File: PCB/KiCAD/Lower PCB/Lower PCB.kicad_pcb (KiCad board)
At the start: 2 copper layers, 188.6 x 165.4 mm, 114 parts, among them IC1 ADG608BRZ, IC2 ADG608BRZ, IC3 ADG608BRZ, Q1 SFH320, Q10 SFH320, Q11 SFH320, Q12 SFH320, Q13 SFH320, Q14 SFH320, Q15 SFH320, Q16 SFH320, Q17 SFH320, Q18 SFH320, Q19 SFH320, Q2 SFH320, Q20 SFH320, Q21 SFH320, Q22 SFH320, Q23 SFH320, Q24 SFH320, Q3 SFH320, Q4 SFH320, Q5 SFH320, Q6 SFH320, Q7 SFH320, Q8 SFH320, Q9 SFH320

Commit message: Work on the lower PCB
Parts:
- added J1: Conn_01x04_MountingPin, Connector_JST:JST_PH_B4B-PH-SM4-TB_1x04-1MP_P2.00mm_Vertical, F.Cu at (-23.8, 40.2)
- added J2: Conn_01x04_MountingPin, Connector_JST:JST_PH_B4B-PH-SM4-TB_1x04-1MP_P2.00mm_Vertical, F.Cu at (-54.6, -19.5)
- added J3: Conn_01x04_MountingPin, Connector_JST:JST_PH_B4B-PH-SM4-TB_1x04-1MP_P2.00mm_Vertical, F.Cu at (62.1, -1.75)
- added J4: Conn_01x02_MountingPin, Connector_JST:JST_PH_B2B-PH-SM4-TB_1x02-1MP_P2.00mm_Vertical, F.Cu at (-35.9, 40.0)
- moved D21 12.8 mm to (-107.0, -89.8)
- moved D22 12.8 mm to (-107.0, -85.2)
- moved D23 12.8 mm to (-107.0, -80.7)
- moved D24 12.8 mm to (-107.0, -76.1)
- moved D25 12.8 mm to (-107.0, -71.5)
- moved D26 12.8 mm to (-107.0, -67.0)
- moved D27 12.8 mm to (-113.1, -89.8)
- moved D28 12.8 mm to (-113.1, -85.2)
- moved D29 12.8 mm to (-113.1, -80.7)
- moved D30 12.8 mm to (-113.1, -76.1)
- moved IC3 9.94 mm to (-73.5, -58.7)
- moved Q17 6.00 mm to (-94.2, -71.5)
- moved Q18 6.00 mm to (-94.2, -67.0)
- moved C3 4.37 mm to (-73.5, -65.5)

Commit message: Started aranging the LDRs and LEDs
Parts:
- moved IC3 129.7 mm to (49.5, -17.4)
- moved D5 74.8 mm to (-59.8, 56.5)
- moved R5 63.3 mm to (-59.8, 51.8)
- moved D10 60.9 mm to (-125.1, 13.8), turned to 0 degrees
- moved D6 57.4 mm to (-125.0, -26.3), turned to 0 degrees
- moved Q5 54.6 mm to (-125.1, 8.85), turned to 0 degrees
- moved Q8 51.4 mm to (-125.0, -21.2), turned to 0 degrees
- moved D9 49.3 mm to (-125.0, 3.75), turned to 0 degrees
- moved D7 47.0 mm to (-125.0, -16.2), turned to 0 degrees
- moved R24 46.9 mm to (-52.5, 51.8)
- moved Q6 45.7 mm to (-125.0, -1.25), turned to 0 degrees
- moved Q7 44.4 mm to (-125.0, -11.2), turned to 0 degrees
- moved D8 43.9 mm to (-125.0, -6.25)
- moved D11 41.8 mm to (-20.0, -107.0), turned to -90 degrees
- moved D15 41.7 mm to (20.0, -107.0), turned to -90 degrees
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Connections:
- IC1 pad 1: unconnected-(IC1-A0-Pad1) -> LED_1_A0
- IC1 pad 15: unconnected-(IC1-A2-Pad15) -> LED_1_A2
- IC1 pad 16: unconnected-(IC1-A1-Pad16) -> LED_1_A1
- IC1 pad 8: unconnected-(IC1-D-Pad8) -> LED_1_OUT
- IC2 pad 1: unconnected-(IC2-A0-Pad1) -> LED_2_A0
- IC2 pad 15: unconnected-(IC2-A2-Pad15) -> LED_2_A2
- IC2 pad 16: unconnected-(IC2-A1-Pad16) -> LED_2_A1
- IC2 pad 8: unconnected-(IC2-D-Pad8) -> LED_2_OUT
- IC3 pad 1: unconnected-(IC3-A0-Pad1) -> LED_3_A0
- IC3 pad 15: unconnected-(IC3-A2-Pad15) -> LED_3_A2
- IC3 pad 16: unconnected-(IC3-A1-Pad16) -> LED_3_A1
- IC3 pad 8: unconnected-(IC3-D-Pad8) -> LED_3_OUT

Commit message: More chnages to LED positions and annotations
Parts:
- moved D20 249.7 mm to (-106.8, -112.0), turned to 0 degrees
- moved D19 239.8 mm to (-106.8, -102.0), turned to 0 degrees
- moved R20 234.1 mm to (-100.8, -112.0), turned to 0 degrees
- moved D18 231.3 mm to (-106.8, -92.0), turned to 0 degrees
- moved Q16 231.1 mm to (-106.8, -77.0), turned to 0 degrees
- moved R19 226.6 mm to (-100.8, -102.0), turned to 0 degrees
- moved Q15 224.1 mm to (-106.8, -67.0), turned to 0 degrees
- moved D17 224.0 mm to (-106.8, -82.0), turned to 0 degrees
- moved R18 219.9 mm to (-100.8, -92.0), turned to 0 degrees
- moved Q14 218.5 mm to (-106.8, -57.0), turned to 0 degrees
- moved D16 218.4 mm to (-106.8, -72.0), turned to 0 degrees
- moved Q13 214.6 mm to (-106.8, -47.0), turned to 0 degrees
- moved R17 214.1 mm to (-100.8, -82.0), turned to 0 degrees
- moved R43 210.6 mm to (-82.5, -114.2)
- moved R44 210.6 mm to (-82.5, -109.2)
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- renumbered J4 to J1, J1 to J2, J2 to J3, J3 to J4, R29 to R21, R30 to R22, R31 to R23, R32 to R24, R33 to R25, R34 to R26, R35 to R27, R36 to R28, R37 to R29, R38 to R30, R21 to R31, R22 to R32, R23 to R33, R24 to R34, R25 to R35, R26 to R36, R27 to R37, R28 to R38

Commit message: Positioned LDRs and LEDs
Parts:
- removed D25, D26, D27, D28, D29, D30: LED, LED_SMD:LED_PLCC-2_3.4x3.0mm_KA
- removed R25, R26, R27, R28, R29, R30: 330, Resistor_SMD:R_0805_2012Metric_Pad1.20x1.40mm_HandSolder
- J3, J4: footprint Connector_JST:JST_PH_B4B-PH-SM4-TB_1x04-1MP_P2.00mm_Vertical -> Connector_JST:JST_PH_S4B-PH-SM4-TB_1x04-1MP_P2.00mm_Horizontal
- moved D21 256.9 mm to (62.8, 42.0), turned to -135 degrees
- moved D22 249.9 mm to (48.8, 55.5), turned to -135 degrees
- moved Q21 233.8 mm to (55.8, 49.0), turned to -135 degrees
- moved Q20 233.0 mm to (70.2, 34.5), turned to -132.33 degrees
- moved D23 232.6 mm to (28.8, 58.2)
- moved R51 232.1 mm to (75.5, 27.5)
- moved D20 229.4 mm to (76.5, 26.0), turned to -120.56 degrees
- moved Q19 224.5 mm to (81.0, 16.0), turned to -103.56 degrees
- moved R50 223.7 mm to (75.5, 17.5)
- moved Q22 222.8 mm to (39.0, 58.2)
- moved R49 221.0 mm to (75.5, 7.50)
- moved R48 218.4 mm to (75.5, -2.50)
- moved D19 218.3 mm to (83.2, 5.50), turned to -96.06 degrees
- moved D24 216.1 mm to (11.5, 58.2)
- moved R47 216.1 mm to (75.5, -12.5)
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
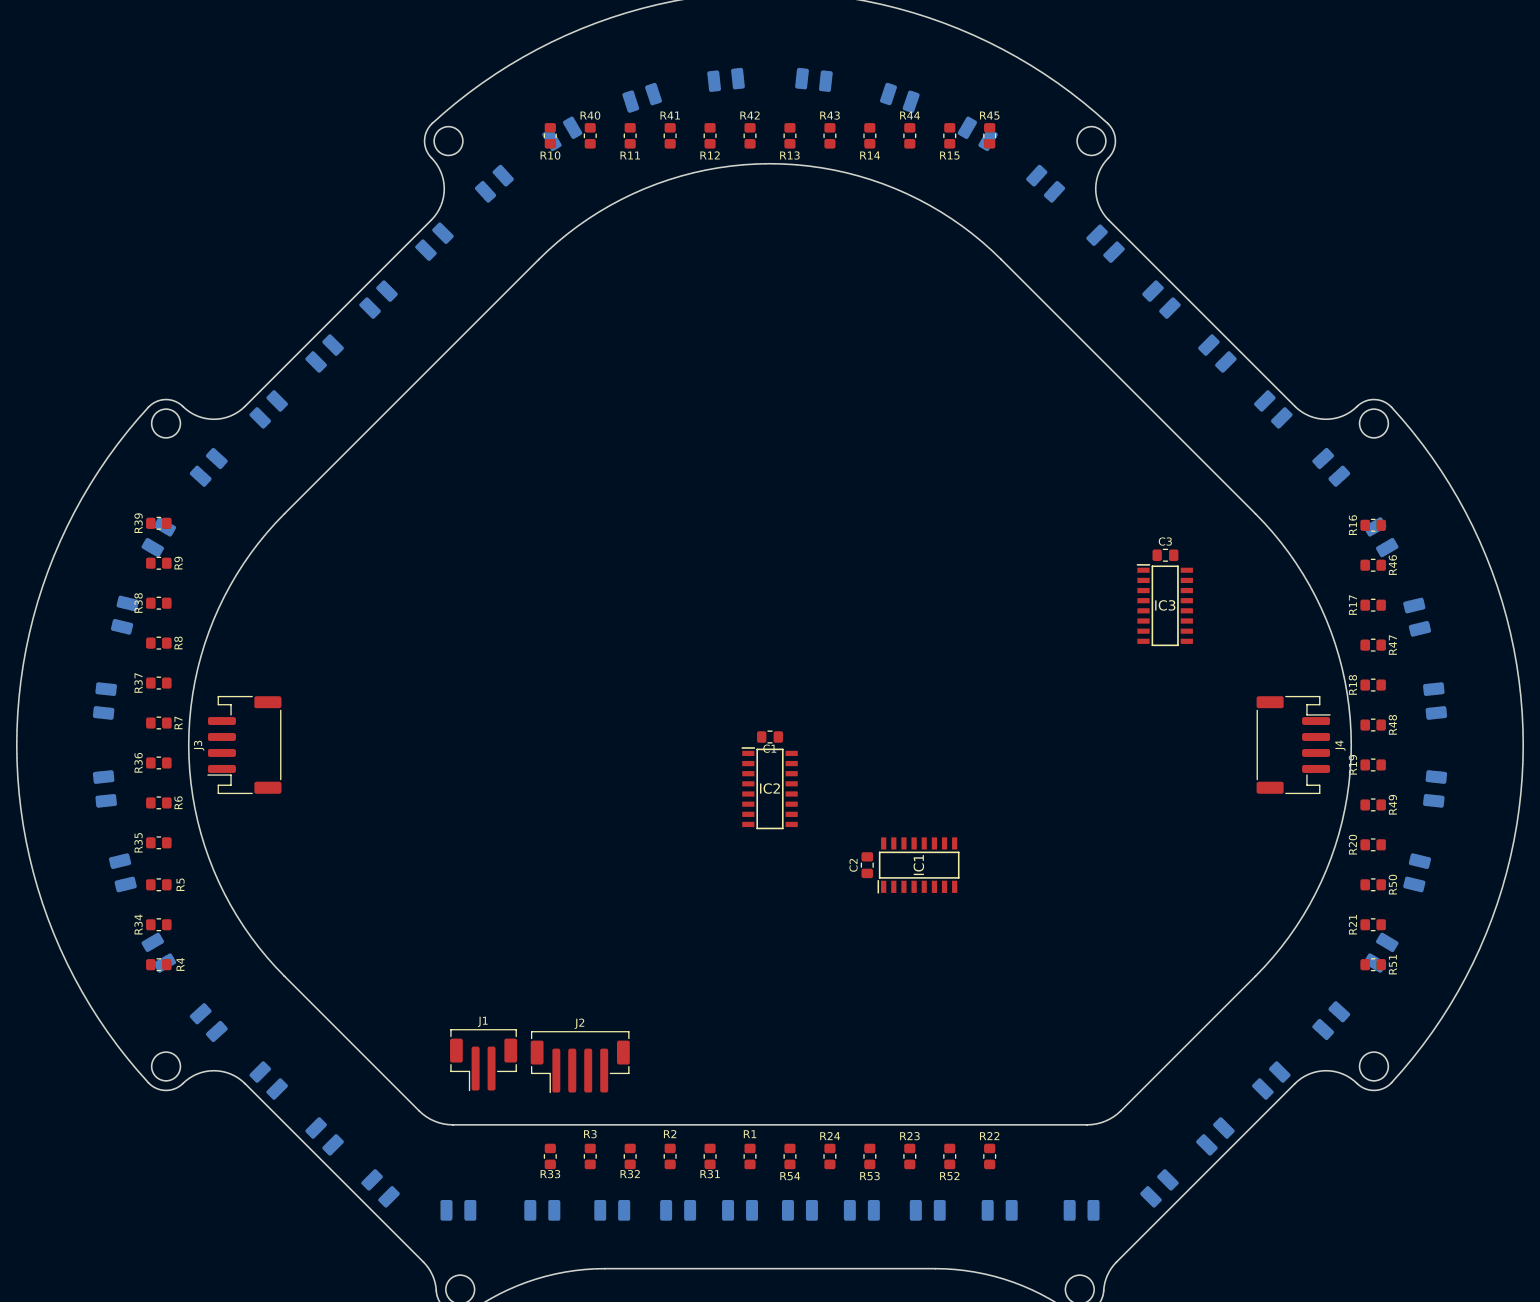
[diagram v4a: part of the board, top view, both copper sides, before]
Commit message: Cleaned up LDR and LED locations
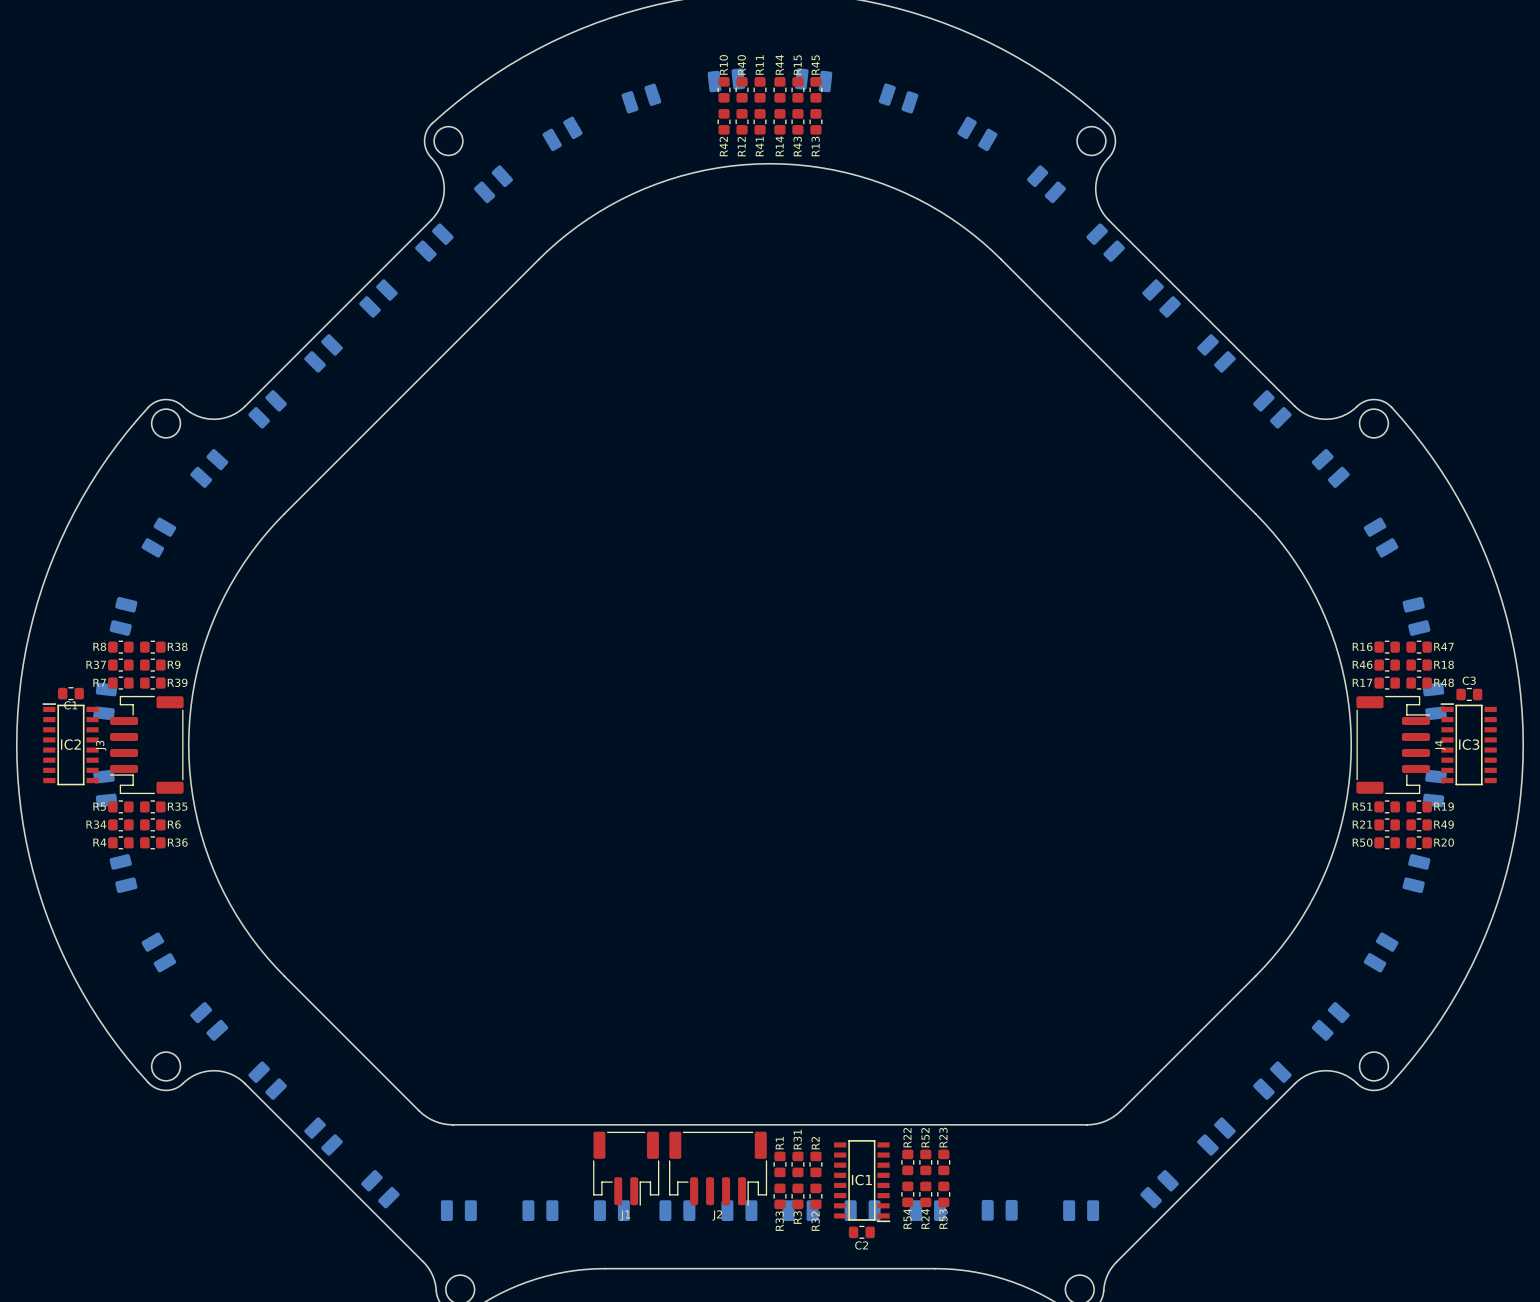
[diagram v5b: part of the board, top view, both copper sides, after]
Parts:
- J1: footprint Connector_JST:JST_PH_B2B-PH-SM4-TB_1x02-1MP_P2.00mm_Vertical -> Connector_JST:JST_PH_S2B-PH-SM4-TB_1x02-1MP_P2.00mm_Horizontal
- J2: footprint Connector_JST:JST_PH_B4B-PH-SM4-TB_1x04-1MP_P2.00mm_Vertical -> Connector_JST:JST_PH_S4B-PH-SM4-TB_1x04-1MP_P2.00mm_Horizontal
- moved IC2 87.7 mm to (-87.5, 0.00)
- moved C1 87.7 mm to (-87.5, -6.42)
- moved C2 46.0 mm to (11.5, 61.0), turned to 180 degrees
- moved C3 41.8 mm to (87.5, -6.33)
- moved IC3 41.8 mm to (87.5, 0.00)
- moved IC1 40.1 mm to (11.5, 54.5), turned to 180 degrees
- moved R33 29.2 mm to (1.25, 56.5), turned to -90 degrees
- moved R3 26.5 mm to (3.50, 56.5)
- moved R32 23.8 mm to (5.75, 56.5)
- moved R10 22.5 mm to (-5.75, -82.0)
- moved R45 22.5 mm to (5.75, -82.0)
- moved J1 22.1 mm to (-18.0, 53.0), turned to 180 degrees
- moved J2 21.5 mm to (-6.50, 53.0), turned to 180 degrees
- moved R39 20.0 mm to (-77.2, -7.75), turned to 0 degrees
- moved R15 19.9 mm to (3.50, -82.0)
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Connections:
- C1 pad 1: +5V -> +3V3
- C2 pad 1: +5V -> +3V3
- C3 pad 1: +5V -> +3V3
- IC1 pad 13: +5V -> +3V3
- IC1 pad 2: +5V -> +3V3
- IC2 pad 13: +5V -> +3V3
- IC2 pad 2: +5V -> +3V3
- IC3 pad 13: +5V -> +3V3
- IC3 pad 2: +5V -> +3V3
- R1 pad 2: +5V -> +3V3
- R10 pad 2: +5V -> +3V3
- R11 pad 2: +5V -> +3V3
- R12 pad 2: +5V -> +3V3
- R13 pad 2: +5V -> +3V3
- R14 pad 2: +5V -> +3V3
- R15 pad 2: +5V -> +3V3
- R16 pad 2: +5V -> +3V3
- R17 pad 2: +5V -> +3V3
- R18 pad 2: +5V -> +3V3
- R19 pad 2: +5V -> +3V3
- R2 pad 2: +5V -> +3V3
- R20 pad 2: +5V -> +3V3
- R21 pad 2: +5V -> +3V3
- R22 pad 2: +5V -> +3V3
- R23 pad 2: +5V -> +3V3
- R24 pad 2: +5V -> +3V3
- R3 pad 2: +5V -> +3V3
- R4 pad 2: +5V -> +3V3
- R5 pad 2: +5V -> +3V3
- R6 pad 2: +5V -> +3V3
- R7 pad 2: +5V -> +3V3
- R8 pad 2: +5V -> +3V3
- R9 pad 2: +5V -> +3V3
